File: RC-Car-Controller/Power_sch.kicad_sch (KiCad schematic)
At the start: 19 parts, among them U2 A6986F3V3TR, U3 LT1963AxST-3.3

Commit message: Fixed Controller PCB
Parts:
- removed C21: 10uF/16V, symbol Device:C
- removed U3: LT1963AxST-3.3, Package_TO_SOT_SMD:SOT-223-3_TabPin2, symbol Regulator_Linear:LT1963AxST-3.3
- added C37: 220pF/25V, Capacitor_SMD:C_0201_0603Metric, symbol Device:C
- added R21: 1.8kohm, Resistor_SMD:R_0201_0603Metric, symbol Device:R
- added R22: 56kohm, Resistor_SMD:R_0201_0603Metric, symbol Device:R
- C1: value 10u/50V -> 1uF/50V; footprint (none) -> Capacitor_SMD:C_0201_0603Metric
- C14: value 20uF/16V -> 10uF/50V; footprint (none) -> Capacitor_SMD:C_1210_3225Metric
- C15: footprint (none) -> Capacitor_SMD:C_1210_3225Metric
- C16, C17, C18, C19, C20, C22: footprint (none) -> Capacitor_SMD:C_0201_0603Metric
- C2: value 10u/50V -> 10uF/50V; footprint (none) -> Capacitor_SMD:C_1210_3225Metric
- C23: value C -> 220pF/16V; footprint (none) -> Capacitor_SMD:C_0201_0603Metric
- L1: value L -> 8.2uH; footprint (none) -> Inductor_SMD:L_Wuerth_MAPI-4030
- R10: value R -> 100kohm; footprint (none) -> Resistor_SMD:R_0201_0603Metric
- R7, R8: footprint (none) -> Resistor_SMD:R_0201_0603Metric
- R9: value R -> 280kohm; footprint (none) -> Resistor_SMD:R_0201_0603Metric
- U2: footprint HTSSOP16_4P5X5P1X0P65P_STM -> footprints:HTSSOP16_4P5X5P1X0P65P_STM
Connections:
- net GNDA: now also R21.1; no longer U2.5 (FSW)
- net GND_3V3: now also C37.1
- net VDD_BATT: now also C1.1
- net at C17.1, U2.2 (VCC), U2.6 (MLF): now also R22.2
- net at R7.2, U2.7 (COMP): now also C37.2
- new net: R21.2, R22.1, U2.5 (FSW)
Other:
- moved on the sheet: C15, C16, C17, C18, C19, C20, C22, C23, L1, R10, R7, R8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

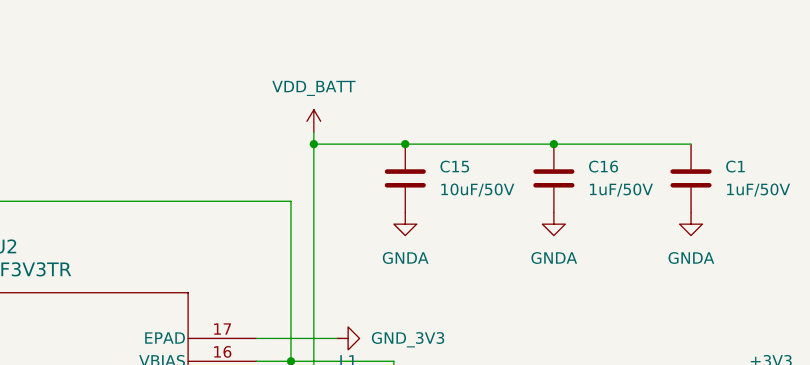
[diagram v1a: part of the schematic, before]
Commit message: Added IO to Controller
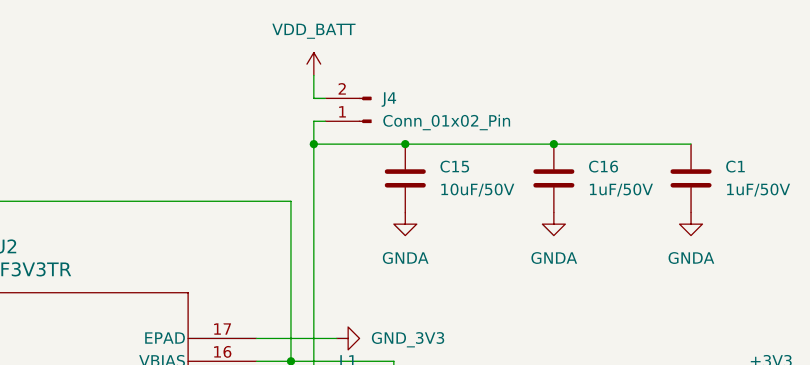
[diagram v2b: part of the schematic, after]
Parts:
- added J4: Conn_01x02_Pin, Connector_PinHeader_2.54mm:PinHeader_1x02_P2.54mm_Vertical, symbol Connector:Conn_01x02_Pin
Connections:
- net VDD_BATT: now also J4.2 (Pin_2); no longer C1.1, C15.1, C16.1, U2.15 (VIN)
- new net: C1.1, C15.1, C16.1, J4.1 (Pin_1), U2.15 (VIN)
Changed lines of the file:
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@@
 	)
 	(junction
-		(at 176.53 78.74)
-		(diameter 0)
-		(color 0 0 0 0)
-	)
-	(junction
 		(at 194.31 107.95)
 		(diameter 0)
@@
 	)
 	(junction
+		(at 176.53 78.74)
+		(diameter 0)
+		(color 0 0 0 0)
+	)
+	(junction
 		(at 170.18 115.57)
 		(diameter 0)
@@
 	(wire
 		(pts
+			(xy 176.53 76.2) (xy 176.53 78.74)
+		)
+		(stroke
+			(width 0)
+			(type default)
+		)
+	)
+	(wire
+		(pts
 			(xy 170.18 118.11) (xy 201.93 118.11)
 		)
@@
 	(wire
 		(pts
+			(xy 177.8 76.2) (xy 176.53 76.2)
+		)
+		(stroke
+			(width 0)
+			(type default)
+		)
+	)
+	(wire
+		(pts
 			(xy 100.33 115.57) (xy 114.3 115.57)
 		)
@@
 	(wire
 		(pts
+			(xy 177.8 73.66) (xy 176.53 73.66)
+		)
+		(stroke
+			(width 0)
+			(type default)
+		)
+	)
+	(wire
+		(pts
 			(xy 114.3 100.33) (xy 114.3 85.09)
 		)
@@
 	(wire
 		(pts
-			(xy 184.15 107.95) (xy 185.42 107.95)
+			(xy 176.53 73.66) (xy 176.53 71.12)
 		)
 		(stroke
@@
 	(wire
 		(pts
-			(xy 95.25 105.41) (xy 114.3 105.41)
+			(xy 184.15 107.95) (xy 185.42 107.95)
 		)
 		(stroke
@@
 	(wire
 		(pts
-			(xy 194.31 120.65) (xy 194.31 121.92)
+			(xy 95.25 105.41) (xy 114.3 105.41)
 		)
 		(stroke
@@
 	(wire
 		(pts
-			(xy 186.69 78.74) (xy 203.2 78.74)
+			(xy 194.31 120.65) (xy 194.31 121.92)
 		)
 		(stroke
@@
 	(wire
 		(pts
-			(xy 176.53 77.47) (xy 176.53 78.74)
+			(xy 186.69 78.74) (xy 203.2 78.74)
 		)
 		(stroke
@@
 	(symbol
 		(lib_id "power:+3V3")
-		(at 176.53 77.47 0)
+		(at 176.53 71.12 0)
 		(unit 1)
 		(exclude_from_sim no)
@@
 		(fields_autoplaced yes)
 		(property "Reference" "#PWR015"
-			(at 176.53 81.28 0)
+			(at 176.53 74.93 0)
 			(effects
 				(font
@@
 		)
 		(property "Value" "VDD_BATT"
-			(at 176.53 72.39 0)
+			(at 176.53 66.04 0)
 			(effects
 				(font
@@
 		)
 		(property "Footprint" ""
-			(at 176.53 77.47 0)
+			(at 176.53 71.12 0)
 			(effects
 				(font
@@
 		)
 		(property "Datasheet" ""
-			(at 176.53 77.47 0)
+			(at 176.53 71.12 0)
 			(effects
 				(font
@@
 		)
 		(property "Description" "Power symbol creates a global label with name \"+3V3\""
-			(at 176.53 77.47 0)
+			(at 176.53 71.12 0)
 			(effects
 				(font
@@
 					(unit 1)
 				)
+			)
+		)
+	)
+	(symbol
+		(lib_id "Connector:Conn_01x02_Pin")
+		(at 182.88 76.2 180)
+		(unit 1)
+		(exclude_from_sim no)
+		(in_bom yes)
+		(on_board yes)
+		(dnp no)
+		(fields_autoplaced yes)
+		(property "Reference" "J4"
+			(at 184.15 73.6599 0)
+			(effects
+				(font
+					(size 1.27 1.27)
+				)
+				(justify right)
+			)
+		)
+		(property "Value" "Conn_01x02_Pin"
+			(at 184.15 76.1999 0)
+			(effects
+				(font
+					(size 1.27 1.27)
+				)
+				(justify right)
+			)
+		)
+		(property "Footprint" "Connector_PinHeader_2.54mm:PinHeader_1x02_P2.54mm_Vertical"
+			(at 182.88 76.2 0)
+			(effects
+				(font
+					(size 1.27 1.27)
+				)
+				(hide yes)
+			)
+		)
+		(property "Datasheet" "~"
+			(at 182.88 76.2 0)
+			(effects
+				(font
+					(size 1.27 1.27)
+				)
+				(hide yes)
+			)
+		)
+		(property "Description" "Generic connector, single row, 01x02, script generated"
+			(at 182.88 76.2 0)
+			(effects
+				(font
+					(size 1.27 1.27)
+				)
+				(hide yes)
+			)
+		)
+		(pin "2"
+		)
+		(pin "1"
+		)
+		(instances
+			(project ""
+				(path "/ba870fd1-751d-4755-8e1a-1ea86ca9e2f6/e8cbdd69-5fc8-4583-a262-8a3c06e86dab"
+					(reference "J4")
+					(unit 1)
+				)

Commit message: Finished prelim. Controller
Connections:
- net VDD_REF: now reaches C1.1, C15.1, C16.1, J4.1 (Pin_1), U2.15 (VIN)
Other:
- moved on the sheet: J4
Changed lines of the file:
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@@
 	)
 	(junction
+		(at 176.53 73.66)
+		(diameter 0)
+		(color 0 0 0 0)
+	)
+	(junction
 		(at 170.18 107.95)
 		(diameter 0)
@@
 	(wire
 		(pts
+			(xy 176.53 73.66) (xy 176.53 78.74)
+		)
+		(stroke
+			(width 0)
+			(type default)
+		)
+	)
+	(wire
+		(pts
 			(xy 82.55 125.73) (xy 100.33 125.73)
 		)
@@
 	(wire
 		(pts
-			(xy 176.53 76.2) (xy 176.53 78.74)
+			(xy 176.53 68.58) (xy 176.53 73.66)
 		)
 		(stroke
@@
 	(wire
 		(pts
-			(xy 177.8 76.2) (xy 176.53 76.2)
+			(xy 177.8 68.58) (xy 176.53 68.58)
 		)
 		(stroke
@@
 	(wire
 		(pts
-			(xy 177.8 73.66) (xy 176.53 73.66)
+			(xy 177.8 66.04) (xy 176.53 66.04)
 		)
 		(stroke
@@
 	(wire
 		(pts
-			(xy 176.53 73.66) (xy 176.53 71.12)
+			(xy 176.53 66.04) (xy 176.53 63.5)
 		)
 		(stroke
@@
 	(symbol
 		(lib_id "power:+3V3")
-		(at 176.53 71.12 0)
+		(at 176.53 63.5 0)
 		(unit 1)
 		(exclude_from_sim no)
@@
 		(fields_autoplaced yes)
 		(property "Reference" "#PWR015"
-			(at 176.53 74.93 0)
+			(at 176.53 67.31 0)
 			(effects
 				(font
@@
 		)
 		(property "Value" "VDD_BATT"
-			(at 176.53 66.04 0)
+			(at 176.53 58.42 0)
 			(effects
 				(font
@@
 		)
 		(property "Footprint" ""
-			(at 176.53 71.12 0)
+			(at 176.53 63.5 0)
 			(effects
 				(font
@@
 		)
 		(property "Datasheet" ""
-			(at 176.53 71.12 0)
+			(at 176.53 63.5 0)
 			(effects
 				(font
@@
 		)
 		(property "Description" "Power symbol creates a global label with name \"+3V3\""
-			(at 176.53 71.12 0)
+			(at 176.53 63.5 0)
 			(effects
 				(font
@@
 	)
 	(symbol
+		(lib_id "power:+3V3")
+		(at 176.53 73.66 270)
+		(unit 1)
+		(exclude_from_sim no)
+		(in_bom yes)
+		(on_board yes)
+		(dnp no)
+		(fields_autoplaced yes)
+		(property "Reference" "#PWR033"
+			(at 172.72 73.66 0)
+			(effects
+				(font
+					(size 1.27 1.27)
+				)
+				(hide yes)
+			)
+		)
+		(property "Value" "VDD_REF"
+			(at 180.34 73.6599 90)
+			(effects
+				(font
+					(size 1.27 1.27)
+				)
+				(justify left)
+			)
+		)
+		(property "Footprint" ""
+			(at 176.53 73.66 0)
+			(effects
+				(font
+					(size 1.27 1.27)
+				)
+				(hide yes)
+			)
+		)
+		(property "Datasheet" ""
+			(at 176.53 73.66 0)
+			(effects
+				(font
+					(size 1.27 1.27)
+				)
+				(hide yes)
+			)
+		)
+		(property "Description" "Power symbol creates a global label with name \"+3V3\""
+			(at 176.53 73.66 0)
+			(effects
+				(font
+					(size 1.27 1.27)
+				)
+				(hide yes)
+			)
+		)
+		(pin "1"
+		)
+		(instances
+			(project "RC-Car-Controller"
+				(path "/ba870fd1-751d-4755-8e1a-1ea86ca9e2f6/e8cbdd69-5fc8-4583-a262-8a3c06e86dab"
+					(reference "#PWR033")
+					(unit 1)
+				)
+			)
+		)
+	)
+	(symbol
 		(lib_id "power:GND")
 		(at 227.33 118.11 0)
@@
 	(symbol
 		(lib_id "Connector:Conn_01x02_Pin")
-		(at 182.88 76.2 180)
+		(at 182.88 68.58 180)
 		(unit 1)
 		(exclude_from_sim no)
@@
 		(fields_autoplaced yes)
 		(property "Reference" "J4"
-			(at 184.15 73.6599 0)
+			(at 184.15 66.0399 0)
 			(effects
 				(font
@@
 		)
 		(property "Value" "Conn_01x02_Pin"
-			(at 184.15 76.1999 0)
+			(at 184.15 68.5799 0)
 			(effects
 				(font
@@
 		)
 		(property "Footprint" "Connector_PinHeader_2.54mm:PinHeader_1x02_P2.54mm_Vertical"
-			(at 182.88 76.2 0)
+			(at 182.88 68.58 0)
 			(effects
 				(font
@@
 		)
 		(property "Datasheet" "~"
-			(at 182.88 76.2 0)
+			(at 182.88 68.58 0)
 			(effects
 				(font
@@
 		)
 		(property "Description" "Generic connector, single row, 01x02, script generated"
-			(at 182.88 76.2 0)
+			(at 182.88 68.58 0)
 			(effects
 				(font

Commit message: Did some stuff on the Controller
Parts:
- removed C1, C16: 1uF/50V, Capacitor_SMD:C_0201_0603Metric, symbol Device:C
- removed C14, C15, C2: 10uF/50V, Capacitor_SMD:C_1210_3225Metric, symbol Device:C
- removed C17: 470nF/25V, Capacitor_SMD:C_0201_0603Metric, symbol Device:C
- removed C18: 220pF/25V, Capacitor_SMD:C_0201_0603Metric, symbol Device:C
- removed C19: 10nF/25V, Capacitor_SMD:C_0201_0603Metric, symbol Device:C
- removed C20: 68nF/25V, Capacitor_SMD:C_0201_0603Metric, symbol Device:C
- removed C22: 1uF/16V, Capacitor_SMD:C_0201_0603Metric, symbol Device:C
- removed C23: 220pF/16V, Capacitor_SMD:C_0201_0603Metric, symbol Device:C
- removed J4: Conn_01x02_Pin, Connector_PinHeader_2.54mm:PinHeader_1x02_P2.54mm_Vertical, symbol Connector:Conn_01x02_Pin
- removed L1: 8.2uH, Inductor_SMD:L_Wuerth_MAPI-4030, symbol Device:L
- removed R10: 100kohm, Resistor_SMD:R_0201_0603Metric, symbol Device:R
- removed R21: 1.8kohm, Resistor_SMD:R_0201_0603Metric, symbol Device:R
- removed R22: 56kohm, Resistor_SMD:R_0201_0603Metric, symbol Device:R
- removed R7: 75kohm, Resistor_SMD:R_0201_0603Metric, symbol Device:R
- removed R8: 1Mohm, Resistor_SMD:R_0201_0603Metric, symbol Device:R
- removed R9: 280kohm, Resistor_SMD:R_0201_0603Metric, symbol Device:R
- removed U2: A6986F3V3TR, footprints:HTSSOP16_4P5X5P1X0P65P_STM, symbol A6986F3V3TR:A6986F3V3TR
- added C35: 1uF/16V, Capacitor_SMD:C_0603_1608Metric, symbol Device:C
- added C36: 100nF/16V, Capacitor_SMD:C_0603_1608Metric, symbol Device:C
- added C38: 22uF/16V, Capacitor_SMD:C_0603_1608Metric, symbol Device:C
- added C39: 10uF/16V, Capacitor_SMD:C_0603_1608Metric, symbol Device:C
- added D3: LED, LED_SMD:LED_0603_1608Metric, symbol Device:LED
- added F1: 2A, symbol Device:Fuse
- added FB1: 100 @ 100MHz, symbol Device:FerriteBead
- added L2: 3.9uH, Inductor_SMD:L_Wuerth_MAPI-4030, symbol Device:L
- added R4: 1.5kohm, Resistor_SMD:R_0603_1608Metric, symbol Device:R
- added R5: 675ohm, Resistor_SMD:R_0603_1608Metric, symbol Device:R
- added U10: STC3100IST, MiniSO8_STM, symbol STC3100IST:STC3100IST
- added U7: BQ21040DBV, Package_TO_SOT_SMD:SOT-23-6, symbol Battery_Management:BQ21040DBV
- added U8: BQ25303JRTER, BQ25303JRTER:RTE0016C, symbol BQ25303JRTER:BQ25303JRTER
- added U9: AP63203WU, Package_TO_SOT_SMD:TSOT-23-6, symbol Regulator_Switching:AP63203WU
- C37: value 220pF/25V -> 22uF/16V; footprint Capacitor_SMD:C_0201_0603Metric -> Capacitor_SMD:C_0603_1608Metric
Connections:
- net GND_3V3 is gone; now on net +3V3: C37.1
- net +3V3: now also C38.1, L2.2, U9.1 (FB)
- net GNDA: now also C35.2, C39.2, R5.2, U7.5 (GND), U9.4 (GND)
- net VDD_BATT: now also F1.1
- net GND_A: now reaches C37.2
- net GND_A: now also C38.2
- new net: R5.1, U7.4 (ISET)
- new net: D3.1 (K), U7.3 (~{CHG})
- new net: D3.2 (A), R4.2
- new net: C39.1, FB1.2, U9.2 (EN), U9.3 (IN)
- new net: F1.2, FB1.1
- new net: C36.1, L2.1, U9.5 (SW)
- new net: C36.2, U9.6 (BST)
- new net VDD_BATT_PRE_SW: R4.1, U7.2 (OUT)
- new net VDD_USB: C35.1, U7.6 (VIN)
- no-connect marks 1 -> 0
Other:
- note added: "10K THERMO"
- note added: "3V3 Regulator"
- note added: "Battery Charger"
- note added: "I saw this on a YT Video lol May be overkill."

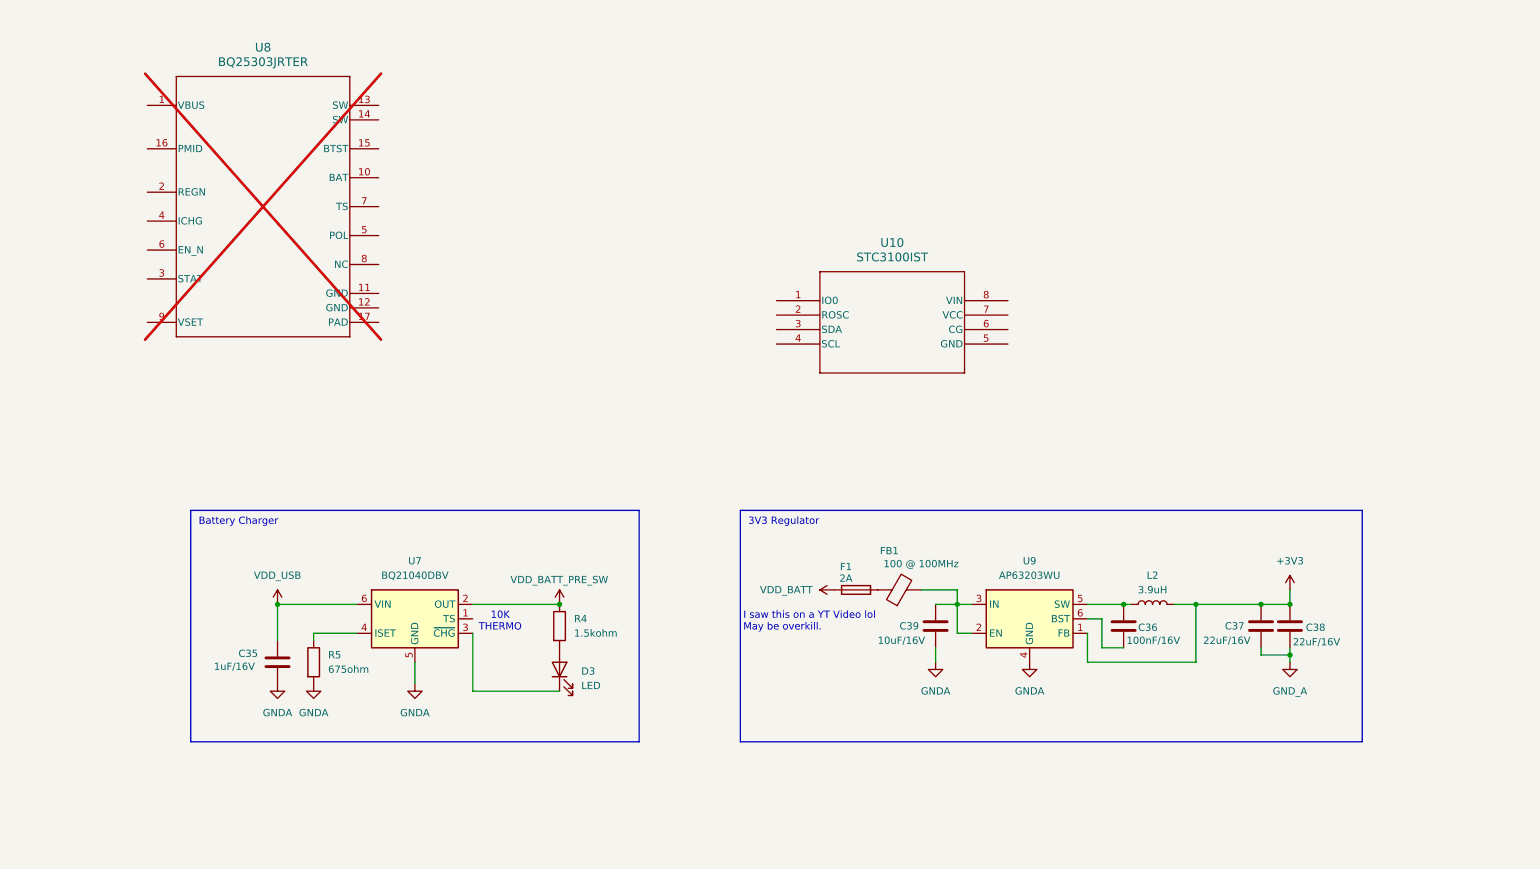
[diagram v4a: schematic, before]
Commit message: Fixed LiPo Charge/Monitor Circuitry
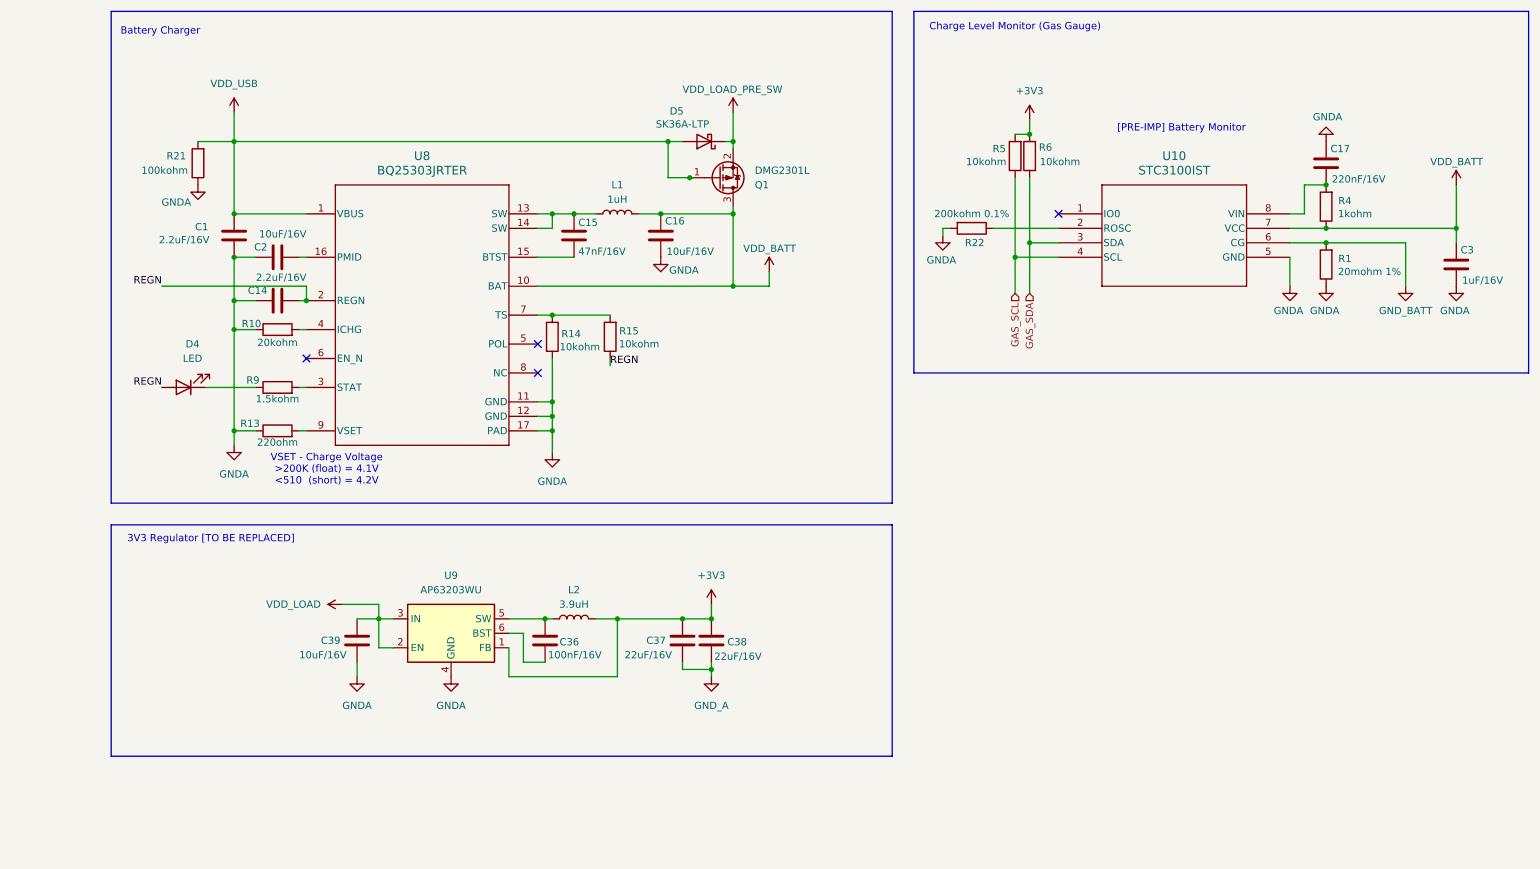
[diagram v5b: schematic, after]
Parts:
- removed C35: 1uF/16V, Capacitor_SMD:C_0603_1608Metric, symbol Device:C
- removed D3: LED, LED_SMD:LED_0603_1608Metric, symbol Device:LED
- removed F1: 2A, symbol Device:Fuse
- removed FB1: 100 @ 100MHz, symbol Device:FerriteBead
- removed U7: BQ21040DBV, Package_TO_SOT_SMD:SOT-23-6, symbol Battery_Management:BQ21040DBV
- added C1, C14: 2.2uF/16V, Capacitor_SMD:C_0603_1608Metric, symbol Device:C
- added C15: 47nF/16V, Capacitor_SMD:C_0603_1608Metric, symbol Device:C
- added C16, C2: 10uF/16V, Capacitor_SMD:C_0603_1608Metric, symbol Device:C
- added C17: 220nF/16V, Capacitor_SMD:C_0603_1608Metric, symbol Device:C
- added C3: 1uF/16V, Capacitor_SMD:C_0603_1608Metric, symbol Device:C
- added D4: LED, LED_SMD:LED_0603_1608Metric, symbol Device:LED
- added D5: SK36A-LTP, Diode_SMD:D_SMA, symbol Device:D_Schottky
- added L1: 1uH, Inductor_SMD:L_Wuerth_MAPI-4030, symbol Device:L
- added Q1: DMG2301L, Package_TO_SOT_SMD:SOT-23, symbol Transistor_FET:DMG2301L
- added R1: 20mohm 1%, Resistor_SMD:R_0603_1608Metric, symbol Device:R
- added R10: 20kohm, Resistor_SMD:R_0603_1608Metric, symbol Device:R
- added R13: 220ohm, Resistor_SMD:R_0603_1608Metric, symbol Device:R
- added R14, R15, R6: 10kohm, Resistor_SMD:R_0603_1608Metric, symbol Device:R
- added R21: 100kohm, Resistor_SMD:R_0603_1608Metric, symbol Device:R
- added R22: 200kohm 0.1%, Resistor_SMD:R_0603_1608Metric, symbol Device:R
- added R9: 1.5kohm, Resistor_SMD:R_0603_1608Metric, symbol Device:R
- R4: value 1.5kohm -> 1kohm
- R5: value 675ohm -> 10kohm
- U8: now fitted; now in the parts list
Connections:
- net VDD_BATT_PRE_SW is gone; now on net VDD_BATT: R4.1
- net +3V3: now also R5.2, R6.2
- net GNDA: now also U10.5 (GND), U8.11 (GND), U8.12 (GND), U8.17 (PAD), C1.2, C14.1, C16.2, C17.1, C2.1, C3.2, R1.1, R10.1, R13.1, R14.2, R21.1, R22.2; no longer R5.2
- net VDD_BATT: now also U10.7 (VCC), U8.10 (BAT), C16.1, C3.1, L1.2, Q1.3 (D)
- net VDD_USB: now also U8.1 (VBUS), C1.1, D5.2 (A), Q1.1 (G), R21.2
- net GAS_SCL: now reaches R5.1
- net GAS_SCL: now also U10.4 (SCL)
- net at R4.2: now also U10.8 (VIN), C17.2
- net at U8.13 (SW): now also U8.14 (SW), C15.1, L1.1
- net at U8.15 (BTST): now also C15.2
- net at U8.16 (PMID): now also C2.2
- net REGN: now reaches U8.2 (REGN)
- net REGN: now also C14.2, D4.2 (A), R15.1
- net at U8.3 (STAT): now also R9.2
- net at U8.4 (ICHG): now also R10.2
- net at U8.7 (TS): now also R14.1, R15.2
- net at U8.9 (VSET): now also R13.2
- net at U10.2 (ROSC): now also R22.1
- net GAS_SDA: now reaches U10.3 (SDA)
- net GAS_SDA: now also R6.1
- net GND_BATT: now reaches U10.6 (CG)
- net GND_BATT: now also R1.2
- net VDD_LOAD: now reaches C39.1, U9.2 (EN), U9.3 (IN)
- new net: D4.1 (K), R9.1
- new net VDD_LOAD_PRE_SW: D5.1 (K), Q1.2 (S)
- no-connect marks 0 -> 4
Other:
- note added: "3V3 Regulator [TO BE REPLACED]"
- note added: "Charge Level Monitor (Gas Gauge)"
- note added: "VSET - Charge Voltage >200K (float) = 4.1V <510 (short) = 4.2V"
- note added: "[PRE-IMP] Battery Monitor"
- note removed: "10K THERMO"
- note removed: "3V3 Regulator"
- note removed: "I saw this on a YT Video lol May be overkill."
- moved on the sheet: C36, C37, C38, C39, L2, U10, U9
